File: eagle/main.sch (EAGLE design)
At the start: 34 parts, among them IC1 TS5205, Q1 SI4840DY, Q5 SI4840DY, U1 SN74AHC1G00DCKR, U2 SN74AHC1G00DCKR, U3 SN74AHC1G00DCKR

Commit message: update routing
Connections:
- net SPI_CS: now also SPI_CON.4; no longer SPI_CON.2
- net SPI_MISO: now also SPI_CON.2; no longer SPI_CON.3
- net SPI_MOSI: now also SPI_CON.3; no longer SPI_CON.4
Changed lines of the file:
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@@
 <net name="SPI_CS" class="0">
+<segment>
+<pinref part="U$2" gate="G$1" pin="2"/>
+<wire x1="208.28" y1="-45.72" x2="190.5" y2="-45.72" width="0.1524" layer="91"/>
+<label x="190.5" y="-45.72" size="1.778" layer="95"/>
+</segment>
+<segment>
+<pinref part="SPI_CON" gate="A" pin="4"/>
+<wire x1="45.72" y1="-60.96" x2="66.04" y2="-60.96" width="0.1524" layer="91"/>
+<label x="55.88" y="-60.96" size="1.778" layer="95"/>
+</segment>
+</net>
+<net name="SPI_MISO" class="0">
+<segment>
+<pinref part="U$2" gate="G$1" pin="8"/>
+<wire x1="208.28" y1="-60.96" x2="190.5" y2="-60.96" width="0.1524" layer="91"/>
+<label x="190.5" y="-60.96" size="1.778" layer="95"/>
+</segment>
 <segment>
 <pinref part="SPI_CON" gate="A" pin="2"/>
@@
 <label x="55.88" y="-55.88" size="1.778" layer="95"/>
 </segment>
+</net>
+<net name="SPI_MOSI" class="0">
 <segment>
-<pinref part="U$2" gate="G$1" pin="2"/>
-<wire x1="208.28" y1="-45.72" x2="190.5" y2="-45.72" width="0.1524" layer="91"/>
-<label x="190.5" y="-45.72" size="1.778" layer="95"/>
+<pinref part="U$2" gate="G$1" pin="7"/>
+<wire x1="208.28" y1="-58.42" x2="190.5" y2="-58.42" width="0.1524" layer="91"/>
+<label x="190.5" y="-58.42" size="1.778" layer="95"/>
 </segment>
-</net>
-<net name="SPI_MISO" class="0">
 <segment>
 <pinref part="SPI_CON" gate="A" pin="3"/>
@@
 <label x="55.88" y="-58.42" size="1.778" layer="95"/>
 </segment>
-<segment>
-<pinref part="U$2" gate="G$1" pin="8"/>
-<wire x1="208.28" y1="-60.96" x2="190.5" y2="-60.96" width="0.1524" layer="91"/>
-<label x="190.5" y="-60.96" size="1.778" layer="95"/>
-</segment>
 </net>
-<net name="SPI_MOSI" class="0">
-<segment>
-<pinref part="SPI_CON" gate="A" pin="4"/>
-<wire x1="45.72" y1="-60.96" x2="66.04" y2="-60.96" width="0.1524" layer="91"/>
-<label x="55.88" y="-60.96" size="1.778" layer="95"/>
-</segment>
-<segment>
-<pinref part="U$2" gate="G$1" pin="7"/>
-<wire x1="208.28" y1="-58.42" x2="190.5" y2="-58.42" width="0.1524" layer="91"/>
-<label x="190.5" y="-58.42" size="1.778" layer="95"/>
-</segment>
-</net>

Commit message: routing
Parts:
- removed SPI_CON: (no value), pinhead:PINHD-1X6
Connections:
- net GND: no longer SPI_CON.1
- net SPI_CS: no longer SPI_CON.4
- net SPI_MISO: no longer SPI_CON.2
- net SPI_MOSI: no longer SPI_CON.3
- net SPI_SCK: no longer SPI_CON.5
- net SPI_V+: no longer SPI_CON.6
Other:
- note added: "SPI connector GND SPI_MISO SPI_MOSI SPI_CS SPI_SCK SPI_V+"
- note removed: "SPI connector"
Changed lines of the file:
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@@
 <part name="SUPPLY2" library="supply2" deviceset="GND" device=""/>
 <part name="U$2" library="Teensy3.0" deviceset="TEENSY_3.0_BASIC-PGM" device=""/>
-<part name="SPI_CON" library="pinhead" deviceset="PINHD-1X6" device=""/>
 <part name="R5" library="resistor" deviceset="R-US_" device="M0805" value="390K"/>
 <part name="R6" library="resistor" deviceset="R-US_" device="M0805" value="100K"/>
@@
 4.9:1 divider</text>
 <text x="254" y="5.08" size="1.778" layer="97">TODO: choose caps</text>
-<text x="40.64" y="-45.72" size="1.778" layer="97">SPI connector</text>
+<text x="38.1" y="-58.42" size="1.778" layer="97">SPI connector
+GND
+SPI_MISO
+SPI_MOSI
+SPI_CS
+SPI_SCK
+SPI_V+</text>
 <text x="40.64" y="10.16" size="1.778" layer="97">TODO: choose connectors</text>
 <text x="365.76" y="-20.32" size="1.778" layer="97">SI4166DY</text>
@@
 <attribute name="VALUE" x="213.106" y="-78.74" size="1.27" layer="96" font="vector" ratio="15"/>
 </instance>
-<instance part="SPI_CON" gate="A" x="43.18" y="-60.96" rot="MR0"/>
 <instance part="R5" gate="G$1" x="408.94" y="-10.16" rot="R270"/>
 <instance part="R6" gate="G$1" x="408.94" y="-25.4" rot="R270"/>
@@
 <wire x1="238.76" y1="-43.18" x2="256.54" y2="-43.18" width="0.1524" layer="91"/>
 <label x="238.76" y="-43.18" size="1.778" layer="95"/>
-</segment>
-<segment>
-<pinref part="SPI_CON" gate="A" pin="1"/>
-<wire x1="45.72" y1="-53.34" x2="66.04" y2="-53.34" width="0.1524" layer="91"/>
-<label x="55.88" y="-53.34" size="1.778" layer="95"/>
 </segment>
 <segment>
@@
 <pinref part="D9" gate="G$1" pin="C"/>
 </segment>
-<segment>
-<pinref part="SPI_CON" gate="A" pin="6"/>
-<wire x1="45.72" y1="-66.04" x2="66.04" y2="-66.04" width="0.1524" layer="91"/>
-<label x="55.88" y="-66.04" size="1.778" layer="95"/>
-</segment>
 </net>
 <net name="SPI_CS" class="0">
@@
 <label x="190.5" y="-45.72" size="1.778" layer="95"/>
 </segment>
-<segment>
-<pinref part="SPI_CON" gate="A" pin="4"/>
-<wire x1="45.72" y1="-60.96" x2="66.04" y2="-60.96" width="0.1524" layer="91"/>
-<label x="55.88" y="-60.96" size="1.778" layer="95"/>
-</segment>
 </net>
 <net name="SPI_MISO" class="0">
@@
 <label x="190.5" y="-60.96" size="1.778" layer="95"/>
 </segment>
-<segment>
-<pinref part="SPI_CON" gate="A" pin="2"/>
-<wire x1="45.72" y1="-55.88" x2="66.04" y2="-55.88" width="0.1524" layer="91"/>
-<label x="55.88" y="-55.88" size="1.778" layer="95"/>
-</segment>
 </net>
 <net name="SPI_MOSI" class="0">
@@
 <wire x1="208.28" y1="-58.42" x2="190.5" y2="-58.42" width="0.1524" layer="91"/>
 <label x="190.5" y="-58.42" size="1.778" layer="95"/>
-</segment>
-<segment>
-<pinref part="SPI_CON" gate="A" pin="3"/>
-<wire x1="45.72" y1="-58.42" x2="66.04" y2="-58.42" width="0.1524" layer="91"/>
-<label x="55.88" y="-58.42" size="1.778" layer="95"/>
 </segment>
 </net>
@@
 <label x="238.76" y="-73.66" size="1.778" layer="95"/>
 </segment>
-<segment>
-<pinref part="SPI_CON" gate="A" pin="5"/>
-<wire x1="45.72" y1="-63.5" x2="66.04" y2="-63.5" width="0.1524" layer="91"/>
-<label x="55.88" y="-63.5" size="1.778" layer="95"/>
-</segment>
-</net>
+</net>

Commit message: frame
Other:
- note added: "https://github.com/texane/psmux"
- note removed: "TODO: choose connectors"
- moved on the sheet: C4, C5, C6, D1, D2, D3, Q1, Q5, R1, R2, R3, R4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

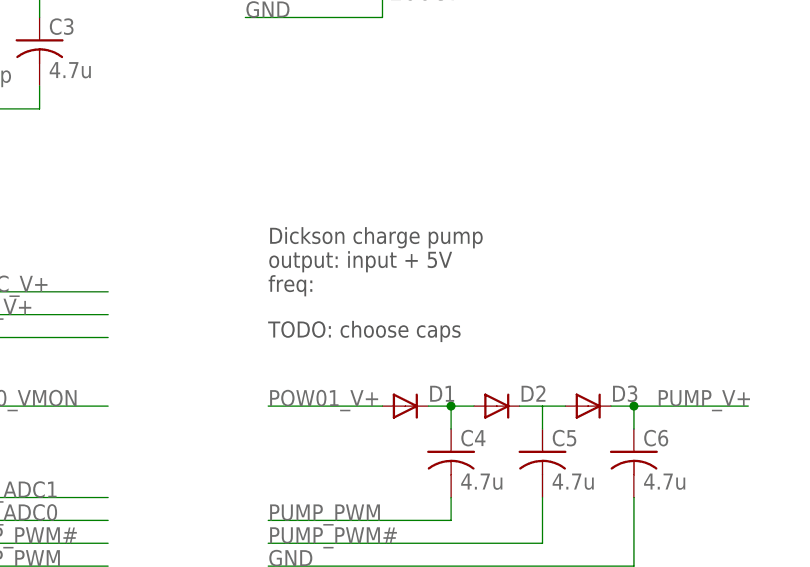
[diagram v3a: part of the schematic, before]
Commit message: remove schematics TODO
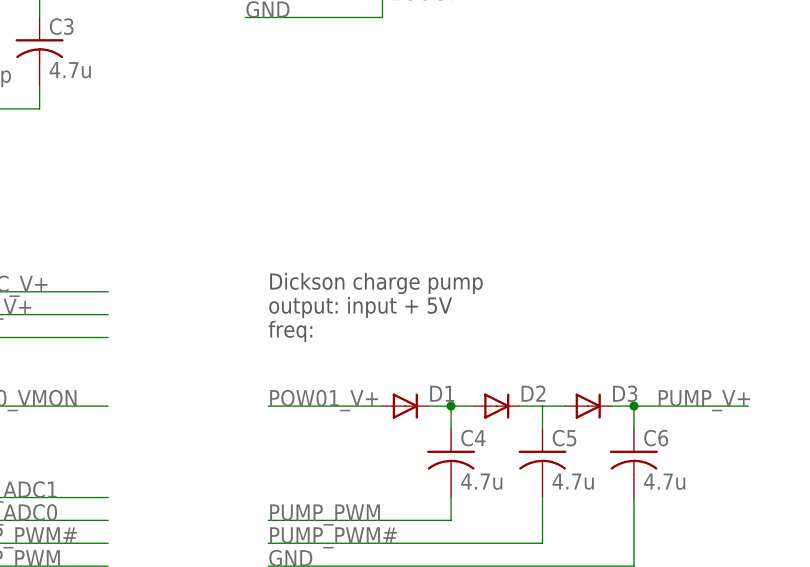
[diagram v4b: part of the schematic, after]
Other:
- note removed: "TODO: choose caps"
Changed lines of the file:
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@@
 output: 4V, 200mA (LDK220)</text>
 <text x="226.06" y="10.16" size="1.778" layer="97">load tank cap</text>
-<text x="228.6" y="-38.1" size="1.778" layer="97">Dickson charge pump
+<text x="228.6" y="-43.18" size="1.778" layer="97">Dickson charge pump
 output: input + 5V
 freq:</text>
@@
 <text x="368.3" y="10.16" size="1.778" layer="97">voltage monitoring paths
 4.9:1 divider</text>
-<text x="228.6" y="-43.18" size="1.778" layer="97">TODO: choose caps</text>
 <text x="38.1" y="-58.42" size="1.778" layer="97">SPI connector
 GND
